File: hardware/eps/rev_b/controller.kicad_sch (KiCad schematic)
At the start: 16 parts, among them J100 SWD_ACCESS_LOGICAL, U100 STM32G0B1KET6N, Y100 ECS-3225MV-160-BN-TR

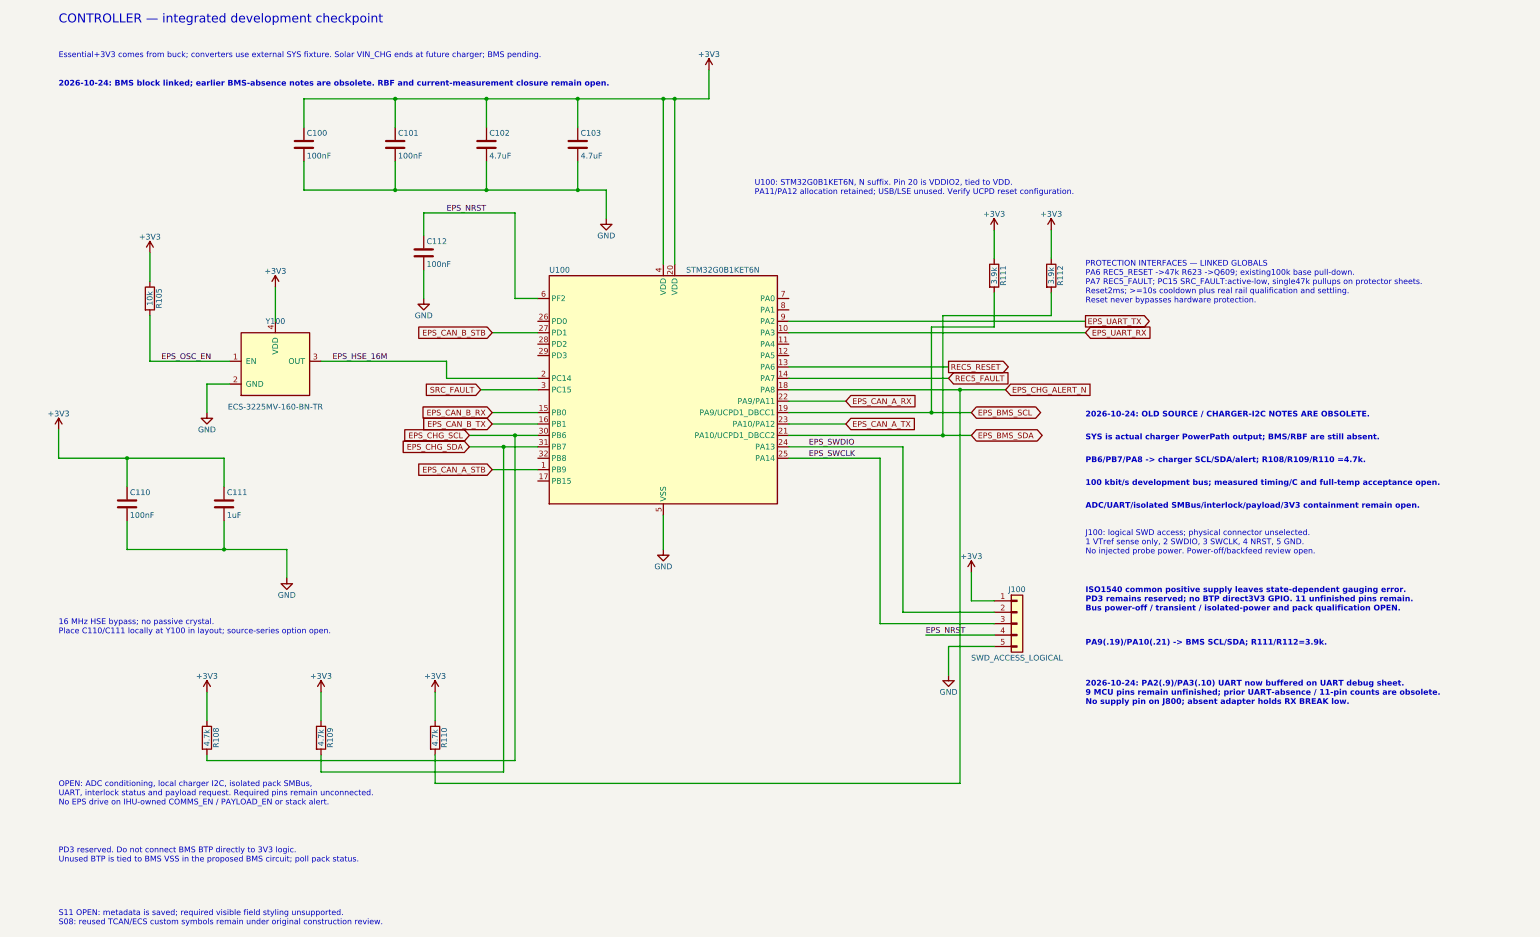
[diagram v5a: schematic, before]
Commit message: Integrate isolated BMS supply and MCU branch recovery controls
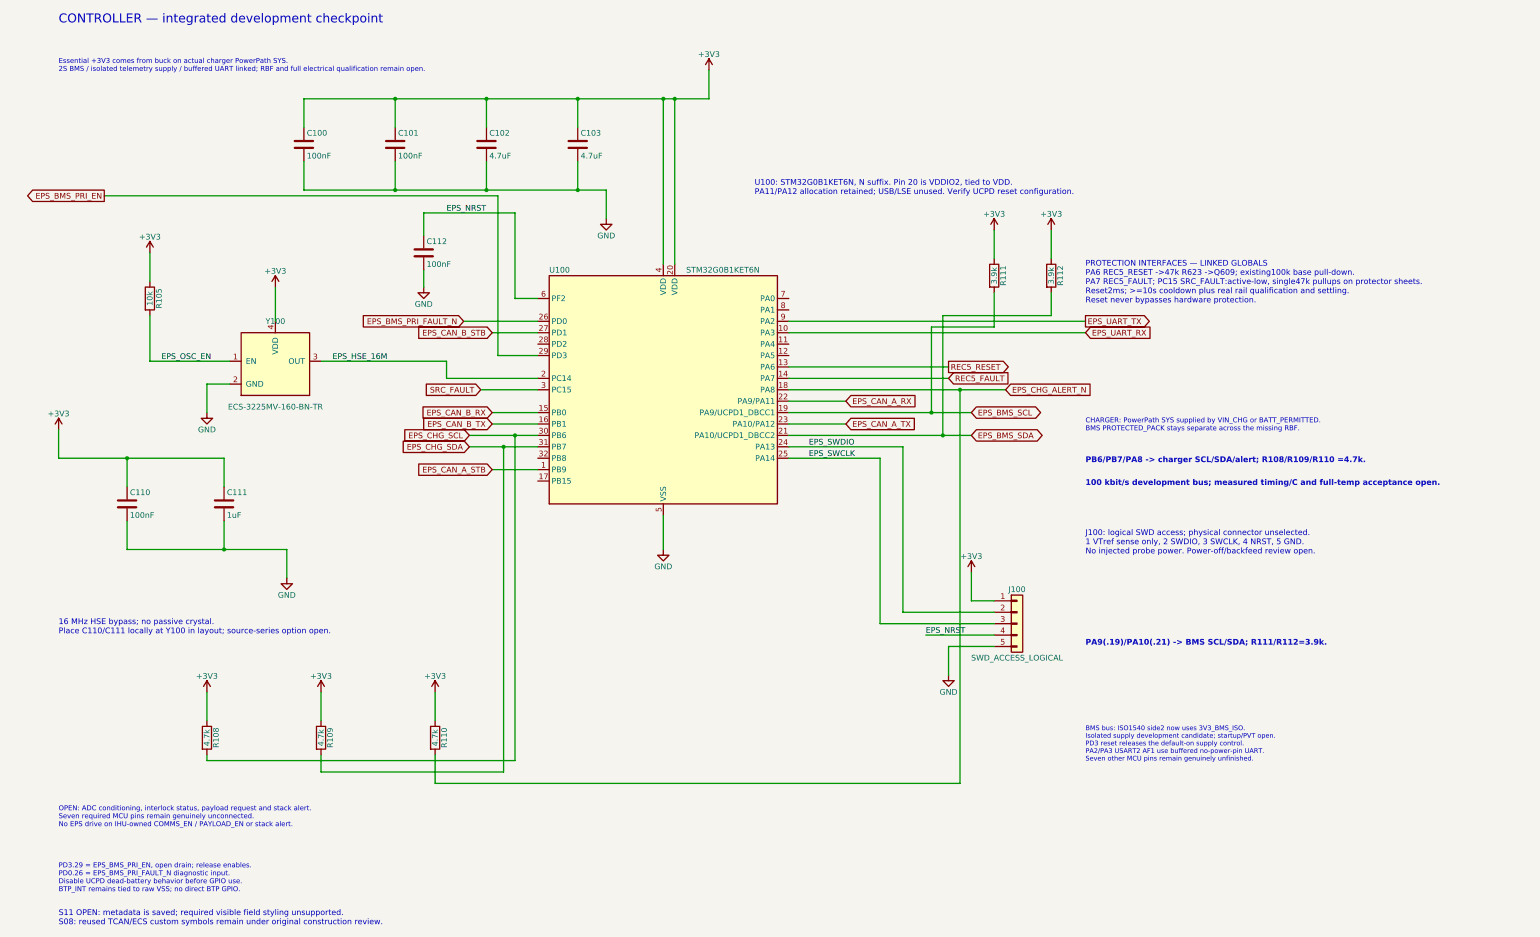
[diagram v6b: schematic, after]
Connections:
- net EPS_BMS_PRI_FAULT_N: now reaches U100.26 (PD0)
- net EPS_BMS_PRI_EN: now reaches U100.29 (PD3)
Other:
- note added: "BMS bus: ISO1540 side2 now uses 3V3_BMS_ISO. Isolated supply development candidate; startup/PVT open. PD3 reset releases the default-on supply control. PA2/PA3 USART2 AF1 use buffered no-power-pin UART. Seven other MCU pins remain genuinely unfinished."
- note added: "CHARGER: PowerPath SYS supplied by VIN_CHG or BATT_PERMITTED. BMS PROTECTED_PACK stays separate across the missing RBF."
- note added: "Essential +3V3 comes from buck on actual charger PowerPath SYS. 2S BMS / isolated telemetry supply / buffered UART linked; RBF and full electrical qualification remain open."
- note added: "OPEN: ADC conditioning, interlock status, payload request and stack alert. Seven required MCU pins remain genuinely unconnected. No EPS drive on IHU-owned COMMS_EN / PAYLOAD_EN or stack alert."
- note added: "PD3.29 = EPS_BMS_PRI_EN, open drain; release enables. PD0.26 = EPS_BMS_PRI_FAULT_N diagnostic input. Disable UCPD dead-battery behavior before GPIO use. BTP_INT remains tied to raw VSS; no direct BTP GPIO."
- note removed: "2026-10-24: BMS block linked; earlier BMS-absence notes are obsolete. RBF and current-measurement closure remain open."
- note removed: "2026-10-24: OLD SOURCE / CHARGER-I2C NOTES ARE OBSOLETE."
- note removed: "2026-10-24: PA2(.9)/PA3(.10) UART now buffered on UART debug sheet. 9 MCU pins remain unfinished; prior UART-absence / 11-pin counts are obsolete. No supply pin on J800; absent adapter holds RX BREAK low."
- note removed: "ADC/UART/isolated SMBus/interlock/payload/3V3 containment remain open."
- note removed: "Essential+3V3 comes from buck; converters use external SYS fixture. Solar VIN_CHG ends at future charger; BMS pending."
- note removed: "ISO1540 common positive supply leaves state-dependent gauging error. PD3 remains reserved; no BTP direct3V3 GPIO. 11 unfinished pins remain. Bus power-off / transient / isolated-power and pack qualification OPEN."
- note removed: "OPEN: ADC conditioning, local charger I2C, isolated pack SMBus, UART, interlock status and payload request. Required pins remain unconnected. No EPS drive on IHU-owned COMMS_EN / PAYLOAD_EN or stack alert."
- note removed: "PD3 reserved. Do not connect BMS BTP directly to 3V3 logic. Unused BTP is tied to BMS VSS in the proposed BMS circuit; poll pack status."
- note removed: "SYS is actual charger PowerPath output; BMS/RBF are still absent."
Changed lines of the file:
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@@
-	(wire
-		(pts
-			(xy 106.68 78.74)
-			(xy 106.68 85.09)
-		)
-	)
 	(wire
 		(pts
@@
 		)
 	)
+	(wire
+		(pts
+			(xy 132.08 90.17)
+			(xy 115.57 90.17)
+		)
+	)
+	(wire
+		(pts
+			(xy 106.68 78.74)
+			(xy 106.68 82.55)
+		)
+	)
+	(wire
+		(pts
+			(xy 132.08 97.79)
+			(xy 123.19 97.79)
+		)
+	)
+	(wire
+		(pts
+			(xy 123.19 97.79)
+			(xy 123.19 62.23)
+		)
+	)
+	(wire
+		(pts
+			(xy 123.19 62.23)
+			(xy 35.56 62.23)
+		)
+	)
 	(text "CONTROLLER — integrated development checkpoint"
 		(at 25.4 24.13 0)
@@
 		)
 	)
-	(text "OPEN: ADC conditioning, local charger I2C, isolated pack SMBus,\nUART, interlock status and payload request. Required pins remain unconnected.\nNo EPS drive on IHU-owned COMMS_EN / PAYLOAD_EN or stack alert."
-		(at 25.4 198.12 0)
-		(effects
-			(font
-				(size 1.27 1.27)
-			)
-			(justify left bottom)
-		)
-	)
-	(text "PD3 reserved. Do not connect BMS BTP directly to 3V3 logic.\nUnused BTP is tied to BMS VSS in the proposed BMS circuit; poll pack status."
-		(at 25.4 210.82 0)
-		(effects
-			(font
-				(size 1.27 1.27)
-			)
-			(justify left bottom)
-		)
-	)
 	(text "S11 OPEN: metadata is saved; required visible field styling unsupported.\nS08: reused TCAN/ECS custom symbols remain under original construction review."
 		(at 25.4 224.79 0)
@@
 		)
 	)
-	(text "Essential+3V3 comes from buck; converters use external SYS fixture. Solar VIN_CHG ends at future charger; BMS pending."
-		(at 25.4 31.75 0)
-		(effects
-			(font
-				(size 1.27 1.27)
-			)
-			(justify left bottom)
-		)
-	)
 	(text "PROTECTION INTERFACES — LINKED GLOBALS\nPA6 REC5_RESET ->47k R623 ->Q609; existing100k base pull-down.\nPA7 REC5_FAULT; PC15 SRC_FAULT:active-low, single47k pullups on protector sheets.\nReset2ms; >=10s cooldown plus real rail qualification and settling.\nReset never bypasses hardware protection."
 		(at 254 86.36 0)
@@
 		)
 	)
-	(text "2026-10-24: OLD SOURCE / CHARGER-I2C NOTES ARE OBSOLETE."
-		(at 254 111.76 0)
-		(effects
-			(font
-				(size 1.27 1.27)
-				(bold yes)
-			)
-			(justify left bottom)
-		)
-	)
-	(text "SYS is actual charger PowerPath output; BMS/RBF are still absent."
-		(at 254 116.84 0)
-		(effects
-			(font
-				(size 1.27 1.27)
-				(bold yes)
-			)
-			(justify left bottom)
-		)
-	)
 	(text "PB6/PB7/PA8 -> charger SCL/SDA/alert; R108/R109/R110 =4.7k."
 		(at 254 121.92 0)
@@
 		)
 	)
-	(text "ADC/UART/isolated SMBus/interlock/payload/3V3 containment remain open."
-		(at 254 132.08 0)
-		(effects
-			(font
-				(size 1.27 1.27)
-				(bold yes)
-			)
-			(justify left bottom)
-		)
-	)
-	(text "2026-10-24: BMS block linked; earlier BMS-absence notes are obsolete. RBF and current-measurement closure remain open."
-		(at 25.4 38.1 0)
-		(effects
-			(font
-				(size 1.27 1.27)
-				(bold yes)
-			)
-			(justify left bottom)
-		)
-	)
-	(text "ISO1540 common positive supply leaves state-dependent gauging error.\nPD3 remains reserved; no BTP direct3V3 GPIO. 11 unfinished pins remain.\nBus power-off / transient / isolated-power and pack qualification OPEN."
-		(at 254 154.94 0)
-		(effects
-			(font
-				(size 1.27 1.27)
-				(bold yes)
-			)
-			(justify left bottom)
-		)
-	)
 	(text "PA9(.19)/PA10(.21) -> BMS SCL/SDA; R111/R112=3.9k."
 		(at 254 162.56 0)
@@
 		)
 	)
+	(text "PD3.29 = EPS_BMS_PRI_EN, open drain; release enables.\nPD0.26 = EPS_BMS_PRI_FAULT_N diagnostic input.\nDisable UCPD dead-battery behavior before GPIO use.\nBTP_INT remains tied to raw VSS; no direct BTP GPIO."
+		(at 25.4 210.82 0)
+		(effects
+			(font
+				(size 1.1 1.1)
+			)
+			(justify left top)
+		)
+	)
+	(text "BMS bus: ISO1540 side2 now uses 3V3_BMS_ISO.\nIsolated supply development candidate; startup/PVT open.\nPD3 reset releases the default-on supply control.\nPA2/PA3 USART2 AF1 use buffered no-power-pin UART.\nSeven other MCU pins remain genuinely unfinished."
+		(at 254 180.34 0)
+		(effects
+			(font
+				(size 1.05 1.05)
+			)
+			(justify left top)
+		)
+	)
+	(text "Essential +3V3 comes from buck on actual charger PowerPath SYS.\n2S BMS / isolated telemetry supply / buffered UART linked; RBF and full electrical qualification remain open."
+		(at 25.4 31.75 0)
+		(effects
+			(font
+				(size 1.1 1.1)
+			)
+			(justify left top)
+		)
+	)
+	(text "CHARGER: PowerPath SYS supplied by VIN_CHG or BATT_PERMITTED.\nBMS PROTECTED_PACK stays separate across the missing RBF."
+		(at 254 111.76 0)
+		(effects
+			(font
+				(size 1.1 1.1)
+			)
+			(justify left top)
+		)
+	)
+	(text "OPEN: ADC conditioning, interlock status, payload request and stack alert.\nSeven required MCU pins remain genuinely unconnected.\nNo EPS drive on IHU-owned COMMS_EN / PAYLOAD_EN or stack alert."
+		(at 25.4 198.12 0)
+		(effects
+			(font
+				(size 1.1 1.1)
+			)
+			(justify left top)
+		)
+	)
 	(label "EPS_NRST"
 		(at 111.76 66.04 0)
@@
 		)
 	)
+	(label "EPS_SWDIO"
+		(at 192.405 118.11 0)
+		(effects
+			(font
+				(size 1.27 1.27)
+			)
+			(justify left bottom)
+		)
+	)
+	(label "EPS_SWCLK"
+		(at 192.405 120.65 0)
+		(effects
+			(font
+				(size 1.27 1.27)
+			)
+			(justify left bottom)
+		)
+	)
+	(label "EPS_NRST"
+		(at 218.44 160.02 0)
+		(effects
+			(font
+				(size 1.27 1.27)
+			)
+			(justify left bottom)
+		)
+	)
 	(label "EPS_HSE_16M"
 		(at 86.36 99.06 0)
-		(effects
-			(font
-				(size 1.27 1.27)
-			)
-			(justify left bottom)
-		)
-	)
-	(label "EPS_SWDIO"
-		(at 192.405 118.11 0)
-		(effects
-			(font
-				(size 1.27 1.27)
-			)
-			(justify left bottom)
-		)
-	)
-	(label "EPS_SWCLK"
-		(at 192.405 120.65 0)
-		(effects
-			(font
-				(size 1.27 1.27)
-			)
-			(justify left bottom)
-		)
-	)
-	(label "EPS_NRST"
-		(at 218.44 160.02 0)
 		(effects
 			(font
@@
 		)
 	)
-  (text "2026-10-24: PA2(.9)/PA3(.10) UART now buffered on UART debug sheet.\n9 MCU pins remain unfinished; prior UART-absence / 11-pin counts are obsolete.\nNo supply pin on J800; absent adapter holds RX BREAK low."
-    (at 254 170.18 0)
-    (effects (font (size 1.27 1.27) (bold yes)) (justify left top))
-  )
+	(global_label "EPS_BMS_PRI_FAULT_N"
+		(shape input)
+		(at 115.57 90.17 180)
+		(effects
+			(font
+				(size 1.27 1.27)
+			)
+			(justify right)
+		)
+	)
+	(global_label "EPS_BMS_PRI_EN"
+		(shape output)
+		(at 35.56 62.23 180)
+		(effects
+			(font
+				(size 1.27 1.27)
+			)
+			(justify right)
+		)
+	)
 	(symbol
 		(lib_id "Ember_EPS_Candidates:ECS_3225MV_DRAFT_v2")
@@
 	(symbol
 		(lib_id "power:GND")
-		(at 106.68 85.09 0)
+		(at 106.68 82.55 0)
 		(unit 1)
 		(in_bom yes)
@@
 		(dnp no)
 		(property "Reference" "#PWR0103"
-			(at 106.68 91.44 0)
+			(at 106.68 88.9 0)
 			(hide yes)
 			(effects
@@
 		)
 		(property "Value" "GND"
-			(at 106.68 88.9 0)
+			(at 106.68 86.36 0)
 			(effects
 				(font
@@
 		)
 		(property "Footprint" ""
-			(at 106.68 85.09 0)
+			(at 106.68 82.55 0)
 			(hide yes)
 			(effects
@@
 		)
 		(property "Datasheet" ""
-			(at 106.68 85.09 0)
+			(at 106.68 82.55 0)
 			(hide yes)
 			(effects
@@
 		)
 		(property "Description" "Power symbol creates a global label with name \"GND\" , ground"
-			(at 106.68 85.09 0)
-			(hide yes)
-			(effects
+			(at 106.68 82.55 0)
+			(hide yes)
+			(effects

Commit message: Integrate supply-qualified SWD and reconcile EMBER stack geometry
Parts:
- removed J100: SWD_ACCESS_LOGICAL, symbol Connector_Generic:Conn_01x05
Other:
- note added: "Physical SWD service on dedicated sheet: six-contact Tag-Connect. EPS_SWDIO / SWCLK / NRST pass through supply-qualified TMUX. No probe target power; connect-under-reset is independent of firmware."
- note removed: "J100: logical SWD access; physical connector unselected. 1 VTref sense only, 2 SWDIO, 3 SWCLK, 4 NRST, 5 GND. No injected probe power. Power-off/backfeed review open."
